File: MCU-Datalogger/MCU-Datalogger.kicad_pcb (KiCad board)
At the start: 2 copper layers, 51.3 x 34 mm, 29 parts, among them J1 Conn_01x04_Pin, J2 Conn_01x04_Pin, J3 Conn_01x09_Pin, J4 Conn_02x03_Odd_Even, U1 24LC1025, U2 24LC1025, U3 DS1337S+, U4 ATMEGA328P-AU, Y1 32.768 KHz, Y2 16 MHz

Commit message: complet 2Layer pcb
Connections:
- J1 pad 4: /SCK -> /SCL
- R3 pad 2: /SCK -> /SCL
- U1 pad 6: /SCK -> /SCL
- U2 pad 6: /SCK -> /SCL
- U3 pad 6: /SCK -> /SCL
- U4 pad 28: /SCK -> /SCL
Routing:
- net /SCL: track 0.00 -> 74.3 mm, vias 0 -> 6
- net /SCK: track 97.4 -> 30.1 mm, vias 3 -> 1
- net GND: track 101.7 -> 111.2 mm
- net Net-(U4-PB7): track 27.6 -> 28.8 mm
- net /Vcc: track 181.1 -> 182.0 mm

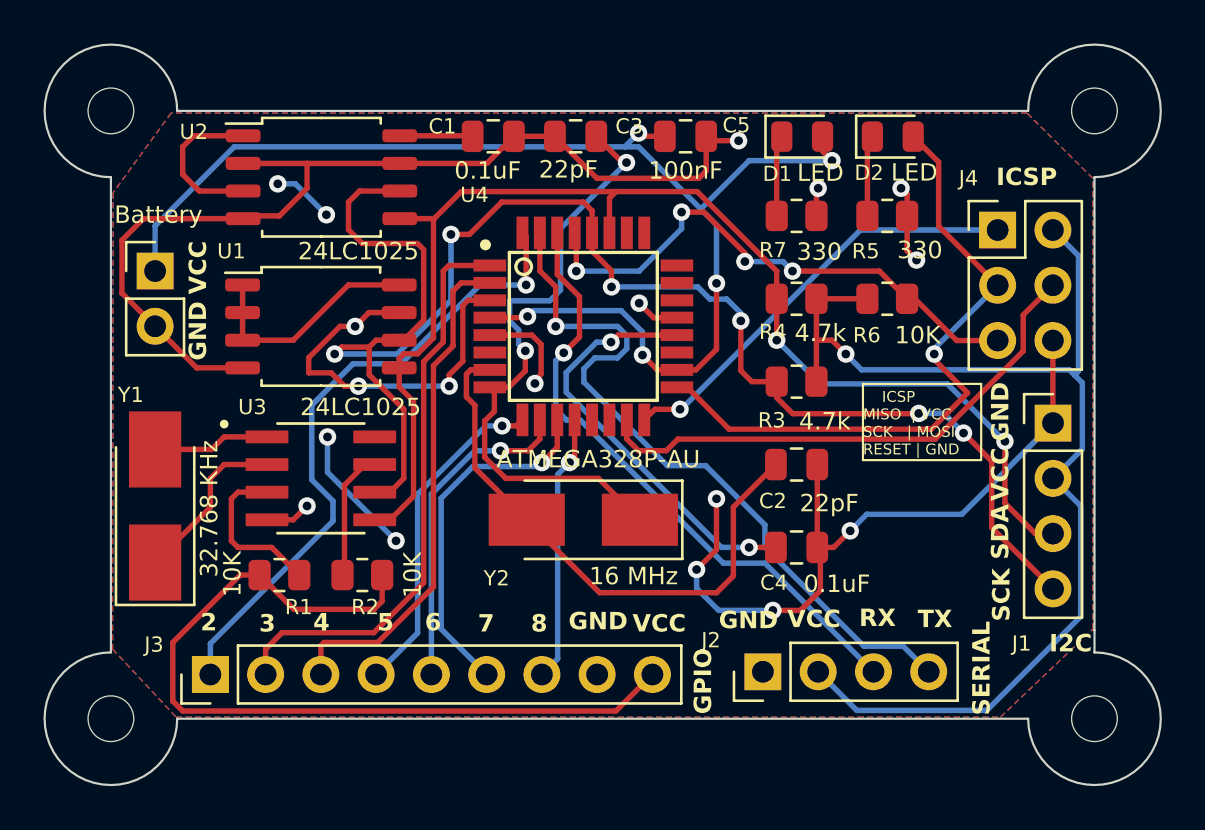
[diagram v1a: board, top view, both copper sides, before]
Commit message: finish 4 Layer design
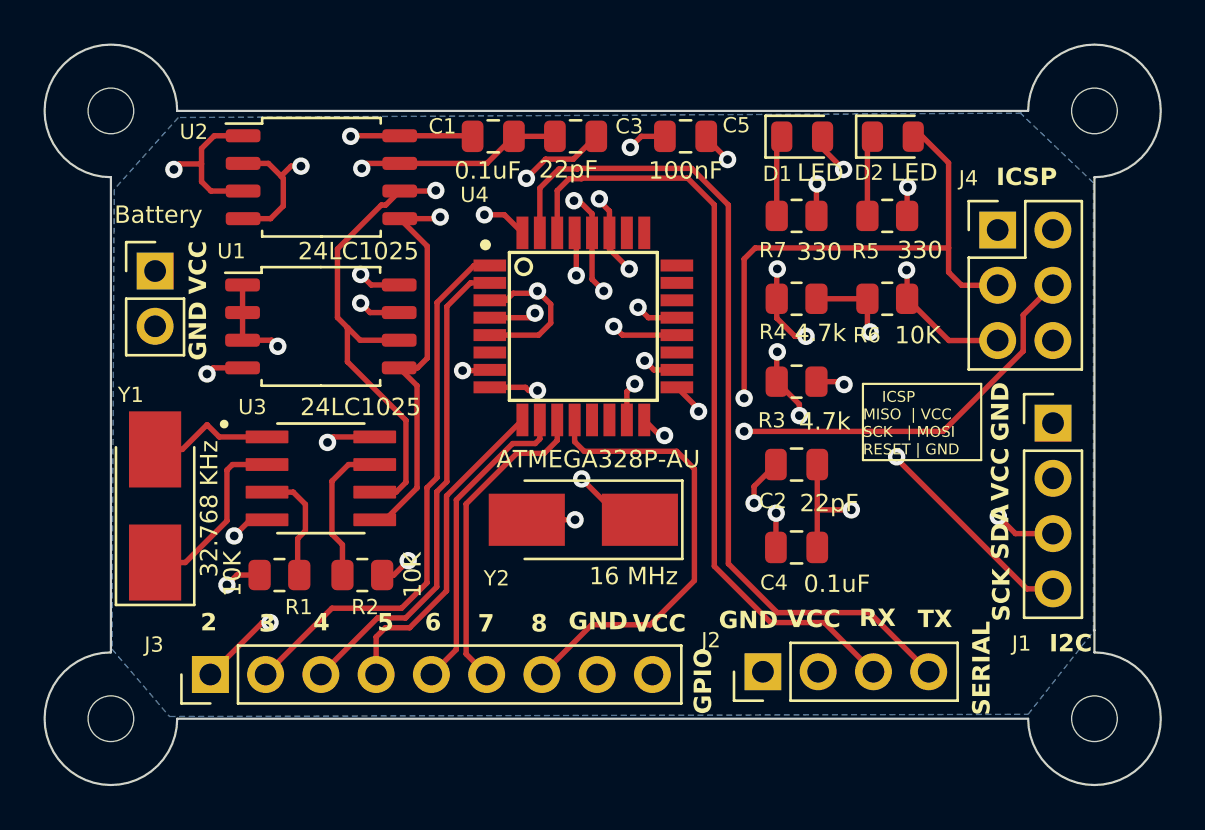
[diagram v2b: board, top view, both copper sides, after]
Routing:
- net /Vcc: track 182.0 -> 43.2 mm, vias 10 -> 13
- net GND: track 111.2 -> 40.4 mm, vias 14 -> 11
- net /SCL: track 74.3 -> 61.9 mm
- net /D8: track 12.3 -> 21.0 mm, vias 1 -> 0
- net /RX: track 28.6 -> 35.8 mm, vias 1 -> 0
- net /TX: track 33.6 -> 39.5 mm, vias 1 -> 0
- net /MISO: track 19.9 -> 23.3 mm
- net /D2: track 29.7 -> 32.9 mm, vias 1 -> 2
- net Net-(U4-PB7): track 28.8 -> 25.8 mm, vias 2 -> 3
- net Net-(U4-PB6): track 26.1 -> 23.2 mm, vias 0 -> 3
- net Net-(U3-~{INTA}): track 7.47 -> 5.42 mm
- net /D7: track 16.5 -> 14.6 mm, vias 1 -> 0
- net /SDA: track 58.9 -> 57.5 mm, vias 2 -> 6
- net /D3: track 26.6 -> 25.4 mm
- net /RESET: track 25.4 -> 24.2 mm, vias 4 -> 2
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- added copper zone on In2.Cu, net /Vcc
- removed copper zone on F.Cu, net /Vcc
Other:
- copper layers 2 -> 4
